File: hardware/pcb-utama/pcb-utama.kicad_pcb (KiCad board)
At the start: 2 copper layers, 100 x 121 mm, 0 parts

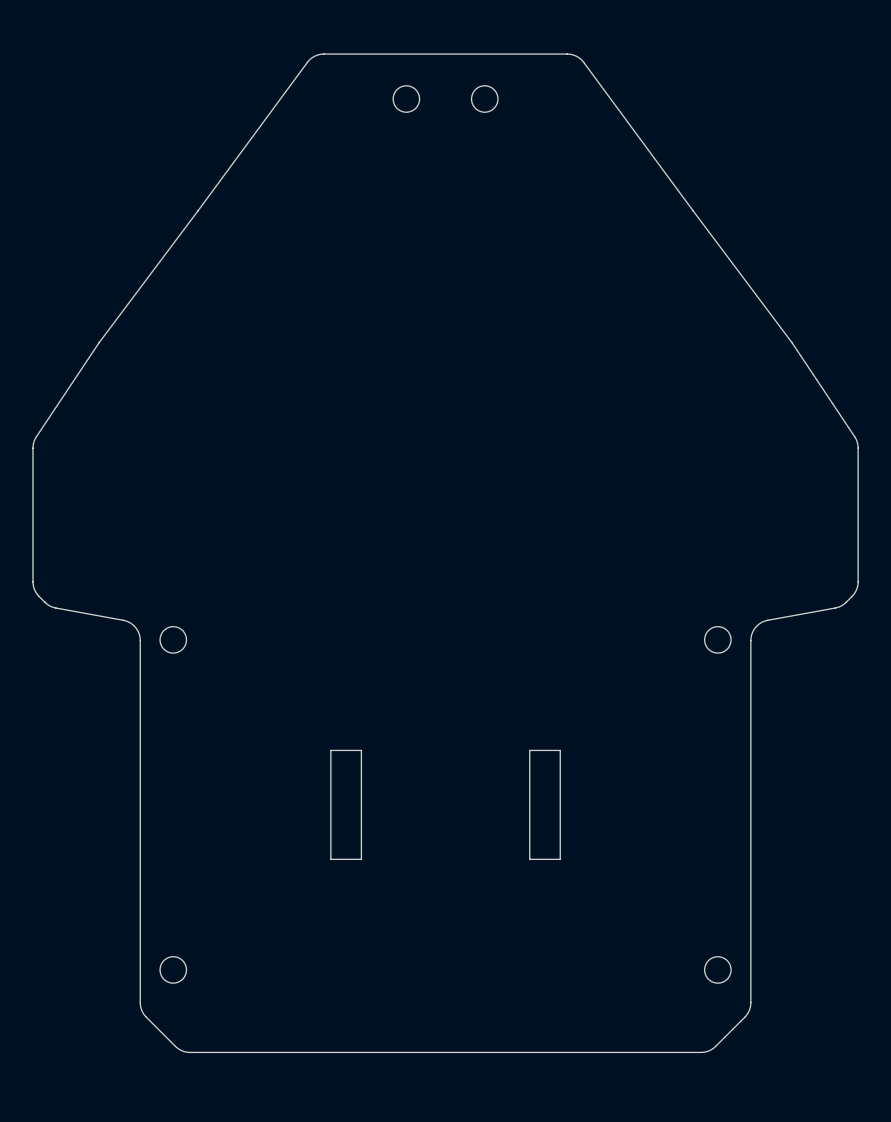
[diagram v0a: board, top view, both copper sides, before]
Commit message: Outline PCB utama bentuk mobil F1
Pilihan user dari 3 opsi: sidepod lebar, pinggang lengkung di antara roda,
hidung panjang (100 x 127 mm). J5 pindah ke sidepod kiri (pin 1 dekat
hidung), elko C1 ke sidepod kiri, kabel sensor menyusuri tepi kiri hidung.
Model v16 (0 tabrakan), render, PCB utama (DRC 0), skematik (ERC 0) dan
dokumen diperbarui.

Co-Authored-By: Claude Opus 5.5 <noreply@anthropic.com>
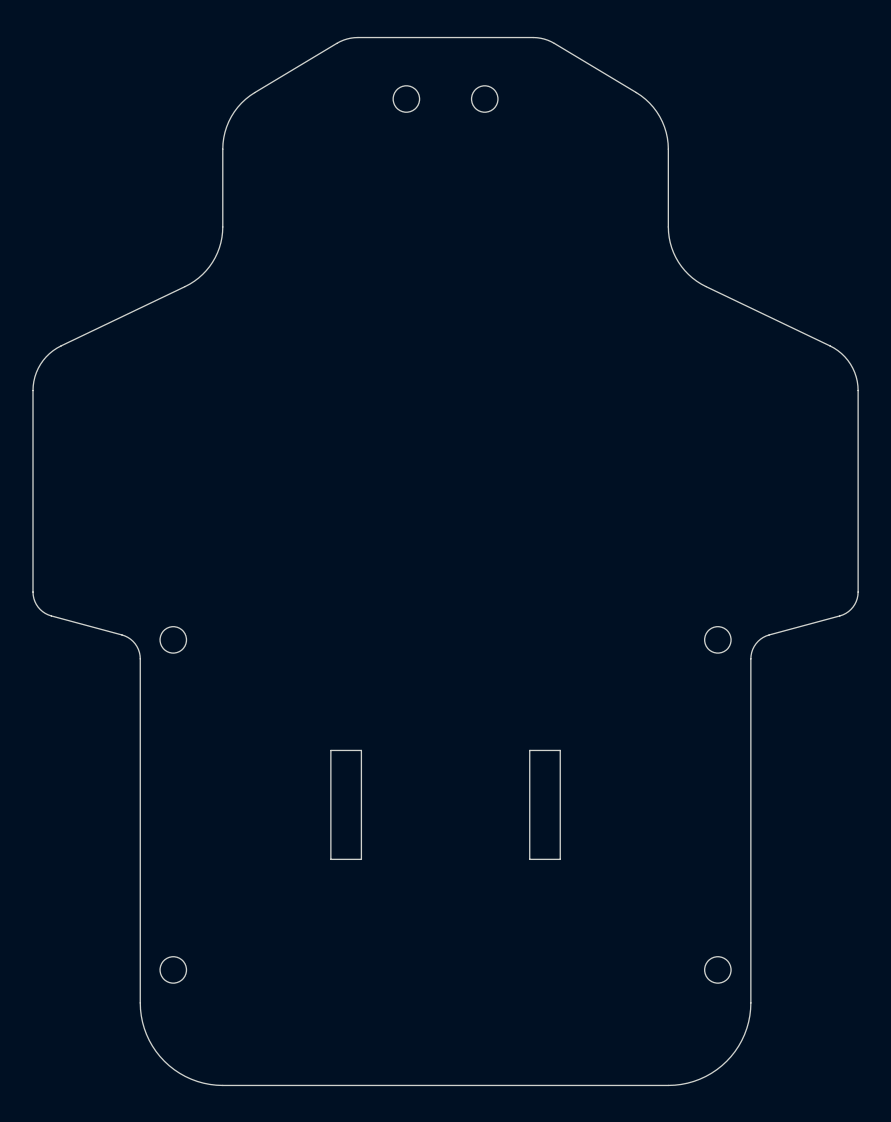
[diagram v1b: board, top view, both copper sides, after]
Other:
- board size 100 x 121 mm -> 100 x 127 mm
- board text added: "C1"

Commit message: Layout PCB utama: penempatan + routing pertama (FreeRouting)
21 footprint ditempatkan sesuai model v16 (bentuk F1), routing FreeRouting
(skrip di hardware/tools/autoroute/), GND pour F.Cu + B.Cu. DRC 0 unconnected;
tersisa 11 error dari footprint pustaka Q1 (TO-92 rapat) dan SW1 (pad
pemasang 0,25 mm), menunggu keputusan user.

Co-Authored-By: Claude Opus 5.5 <noreply@anthropic.com>
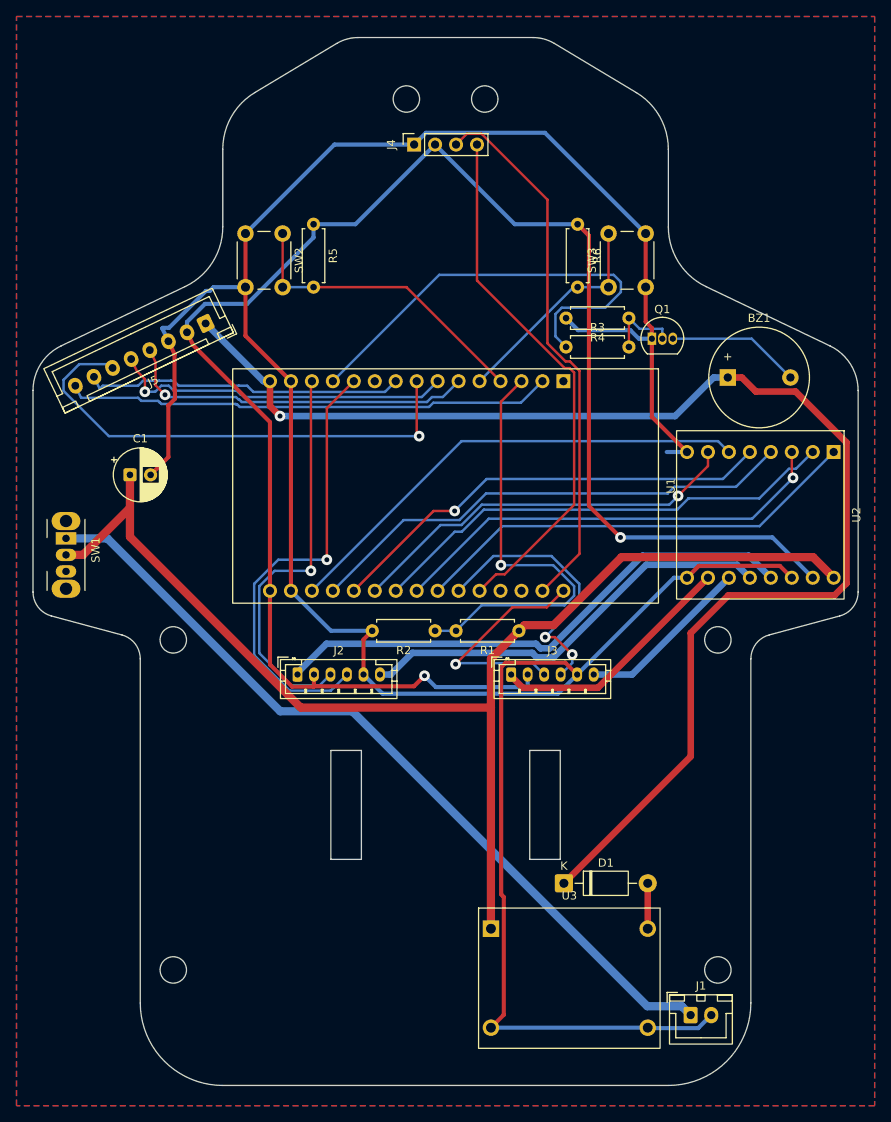
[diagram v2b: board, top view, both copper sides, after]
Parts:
- added BZ1: Buzzer aktif 5V, Buzzer_Beeper:Buzzer_12x9.5RM7.6, F.Cu at (234.2, 128.8)
- added C1: 100uF 16V, Capacitor_THT:CP_Radial_D6.3mm_P2.50mm, F.Cu at (161.8, 140.6)
- added D1: 1N5819, Diode_THT:D_DO-41_SOD81_P10.16mm_Horizontal, F.Cu at (214.3, 190.1)
- added J1: Baterai (P+/P- BMS), Connector_JST:JST_XH_B2B-XH-A_1x02_P2.50mm_Vertical, F.Cu at (229.7, 206.0)
- added J2: Motor kiri + encoder, Connector_JST:JST_PH_B6B-PH-K_1x06_P2.00mm_Vertical, F.Cu at (182.1, 164.8)
- added J3: Motor kanan + encoder, Connector_JST:JST_PH_B6B-PH-K_1x06_P2.00mm_Vertical, F.Cu at (207.9, 164.8)
- added J4: OLED 0,96 I2C, Connector_PinSocket_2.54mm:PinSocket_1x04_P2.54mm_Vertical, F.Cu at (196.2, 100.5)
- added J5: Kabel PCB sensor (= J1 sensor), Connector_JST:JST_XH_B8B-XH-A_1x08_P2.50mm_Vertical, F.Cu at (170.9, 122.2)
- added Q1: S8050, Package_TO_SOT_THT:TO-92_Inline, F.Cu at (225.0, 124.0)
- added R1: 100k, Resistor_THT:R_Axial_DIN0207_L6.3mm_D2.5mm_P7.62mm_Horizontal, F.Cu at (208.9, 159.4)
- added R2: 33k, Resistor_THT:R_Axial_DIN0207_L6.3mm_D2.5mm_P7.62mm_Horizontal, F.Cu at (198.7, 159.4)
- added R3: 1k, Resistor_THT:R_Axial_DIN0207_L6.3mm_D2.5mm_P7.62mm_Horizontal, F.Cu at (214.6, 125.0)
- added R4: 10k, Resistor_THT:R_Axial_DIN0207_L6.3mm_D2.5mm_P7.62mm_Horizontal, F.Cu at (222.2, 121.5)
- added R5: 10k, Resistor_THT:R_Axial_DIN0207_L6.3mm_D2.5mm_P7.62mm_Horizontal, F.Cu at (184.0, 110.2)
- added R6: 10k, Resistor_THT:R_Axial_DIN0207_L6.3mm_D2.5mm_P7.62mm_Horizontal, F.Cu at (216.0, 110.2)
- added SW1: Saklar geser, Button_Switch_THT:SW_Slide_SPDT_Angled_CK_OS102011MA1Q, F.Cu at (154.0, 148.2)
- added SW2: Tombol A, Button_Switch_THT:SW_PUSH_6mm, F.Cu at (180.2, 111.3)
- added SW3: Tombol B, Button_Switch_THT:SW_PUSH_6mm, F.Cu at (219.8, 117.8)
- added U1: ESP32 DevKit 30 pin, ltm:ESP32_DevKit_30P_W25.4, F.Cu at (196.5, 141.9)
- added U2: TB6612 modul, ltm:TB6612_Module_2x8_W15.24, F.Cu at (238.2, 145.4)
- added U3: MP1584 (set 5,0 V), ltm:MP1584_Module, F.Cu at (215.0, 201.6)
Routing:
- net GND: track 0.00 -> 337.5 mm
- net +3V3: track 0.00 -> 208.5 mm, vias 0 -> 2
- net +5V: track 0.00 -> 164.4 mm, vias 0 -> 1
- net VBAT: track 0.00 -> 150.3 mm
- net BAT+: track 0.00 -> 99.6 mm
- net SCL: track 0.00 -> 66.1 mm
- net ML_P: track 0.00 -> 65.0 mm
- net SDA: track 0.00 -> 64.7 mm
- net MUX_S1: track 0.00 -> 60.4 mm, vias 0 -> 1
- net STBY: track 0.00 -> 60.0 mm
- net MUX_SIG: track 0.00 -> 59.3 mm
- net BIN2: track 0.00 -> 58.6 mm
- net AIN2: track 0.00 -> 57.5 mm
- net ENC_L_B: track 0.00 -> 55.5 mm, vias 0 -> 1
- net BUZ: track 0.00 -> 55.4 mm
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- added copper zone on B.Cu, net GND
- added copper zone on F.Cu, net GND
